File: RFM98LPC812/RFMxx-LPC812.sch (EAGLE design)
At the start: 33 parts, among them X1 BU-SMA-V, X2 BU-SMA-V

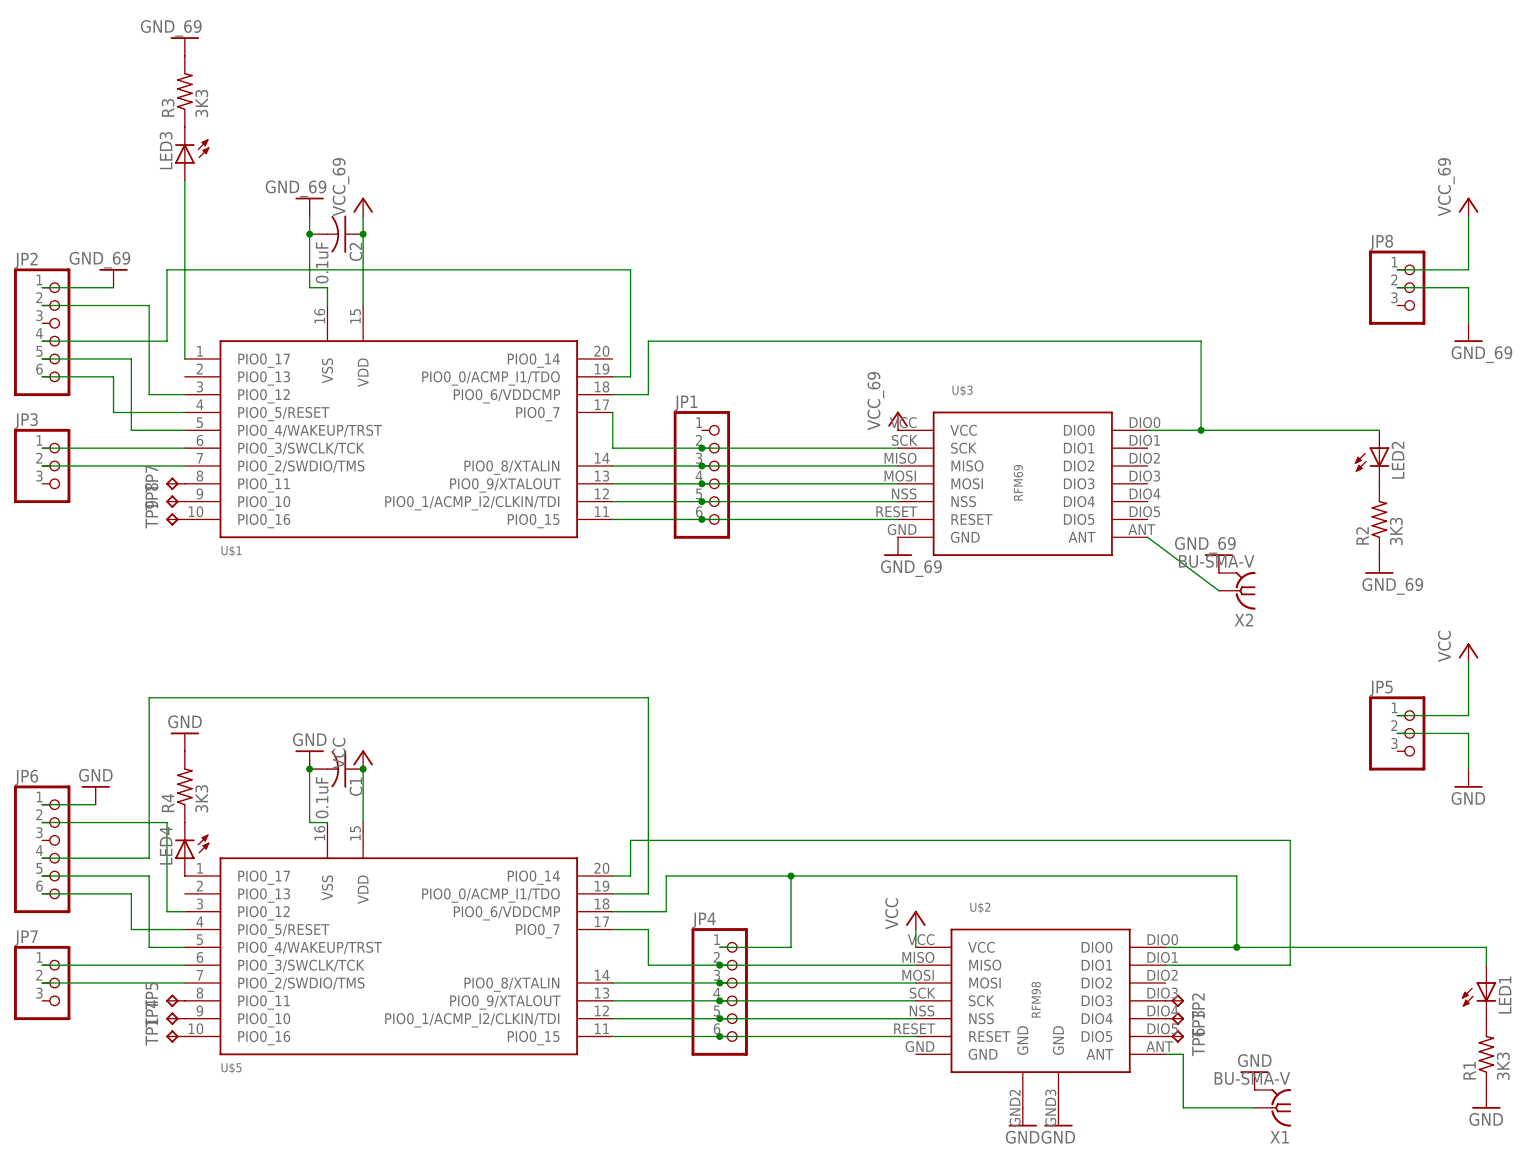
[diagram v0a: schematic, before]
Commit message: added TPs for DIO0..5 on RFM69 side
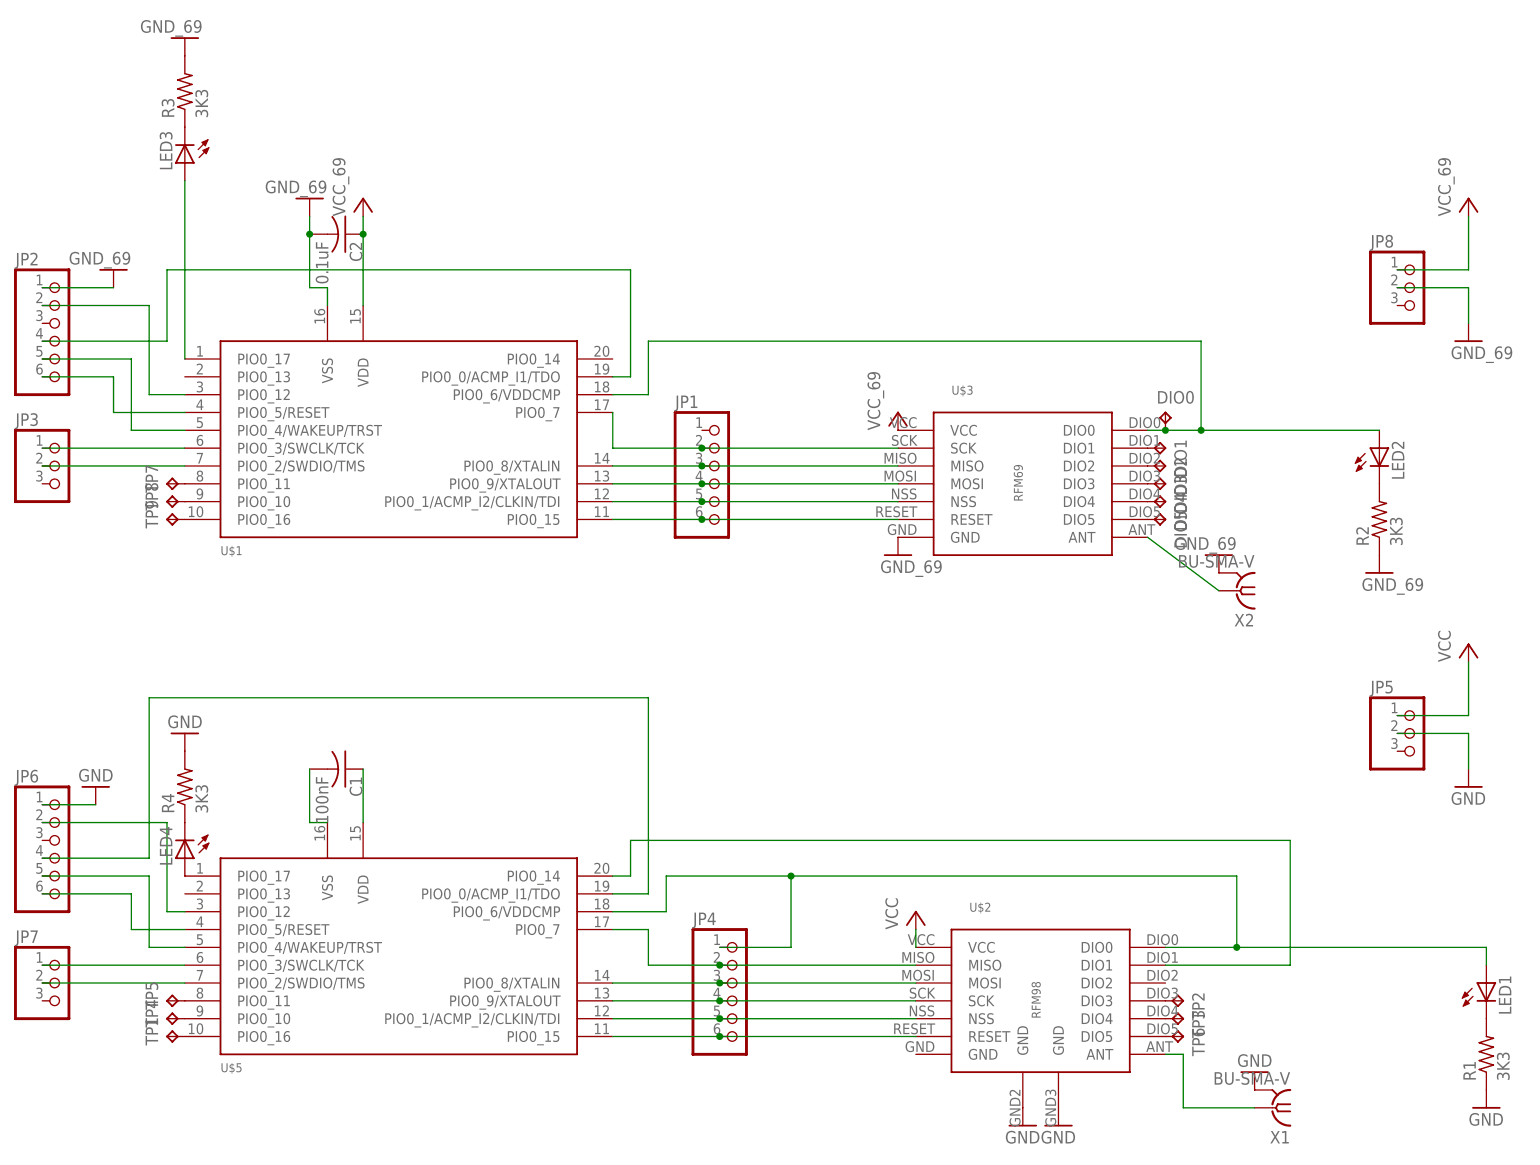
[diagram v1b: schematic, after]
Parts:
- added DIO0, DIO1, DIO2, DIO3, DIO4, DIO5: TPB1,27, testpad:TPB1,27
- C1: value 0.1uF -> 100nF
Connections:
- new net N$45: C1.2, U$5.VSS
- new net N$46: C1.1, U$5.VDD
- new net N$47: DIO1.TP, U$3.DIO1
- new net N$48: DIO2.TP, U$3.DIO2
- new net N$49: DIO3.TP, U$3.DIO3
- new net N$50: DIO4.TP, U$3.DIO4
- new net N$51: DIO5.TP, U$3.DIO5
- net GND: no longer C1.2, U$5.VSS
- net N$24: now also DIO0.TP
- net VCC: no longer C1.1, U$5.VDD
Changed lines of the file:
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@@
 <setting verticaltext="up"/>
 </settings>
-<grid distance="0.1" unitdist="inch" unit="inch" style="lines" multiple="1" display="yes" altdistance="0.01" altunitdist="inch" altunit="inch"/>
+<grid distance="0.1" unitdist="inch" unit="inch" style="lines" multiple="1" display="no" altdistance="0.01" altunitdist="inch" altunit="inch"/>
 <layers>
 <layer number="1" name="Top" color="4" fill="1" visible="no" active="no"/>
@@
 <part name="U$5" library="LPC812" deviceset="LPC812M101JD20" device=""/>
 <part name="JP4" library="adafruit" deviceset="PINHD-1X6" device=""/>
-<part name="P+1" library="supply1" deviceset="VCC" device=""/>
 <part name="JP5" library="adafruit" deviceset="PINHD-1X3" device=""/>
 <part name="P+3" library="supply1" deviceset="VCC" device=""/>
@@
 <part name="GND_RFM2" library="supply1" deviceset="GND" device=""/>
 <part name="GND_RFM3" library="supply1" deviceset="GND" device=""/>
-<part name="C1" library="adafruit" deviceset="C-US" device="C0805" value="0.1uF"/>
+<part name="C1" library="adafruit" deviceset="C-US" device="C0805" value="100nF"/>
 <part name="TP1" library="testpad" deviceset="TP" device="B1,27"/>
 <part name="JP7" library="adafruit" deviceset="PINHD-1X3" device=""/>
@@
 <part name="TP8" library="testpad" deviceset="TP" device="B1,27"/>
 <part name="TP9" library="testpad" deviceset="TP" device="B1,27"/>
-<part name="GND_RFM1" library="supply1" deviceset="GND" device=""/>
+<part name="DIO1" library="testpad" deviceset="TP" device="B1,27"/>
+<part name="DIO2" library="testpad" deviceset="TP" device="B1,27"/>
+<part name="DIO3" library="testpad" deviceset="TP" device="B1,27"/>
+<part name="DIO4" library="testpad" deviceset="TP" device="B1,27"/>
+<part name="DIO5" library="testpad" deviceset="TP" device="B1,27"/>
+<part name="DIO0" library="testpad" deviceset="TP" device="B1,27"/>
 </parts>
 <sheets>
@@
 <instance part="U$5" gate="G$1" x="-91.44" y="-27.94"/>
 <instance part="JP4" gate="A" x="-40.64" y="-33.02"/>
-<instance part="P+1" gate="VCC" x="-93.98" y="2.54"/>
 <instance part="JP5" gate="A" x="55.88" y="5.08"/>
 <instance part="P+3" gate="VCC" x="63.5" y="17.78"/>
@@
 <instance part="TP8" gate="G$1" x="-121.92" y="38.1" rot="R90"/>
 <instance part="TP9" gate="G$1" x="-121.92" y="35.56" rot="R90"/>
-<instance part="GND_RFM1" gate="1" x="-101.6" y="2.54" rot="R180"/>
+<instance part="DIO1" gate="G$1" x="20.32" y="45.72" rot="R270"/>
+<instance part="DIO2" gate="G$1" x="20.32" y="43.18" rot="R270"/>
+<instance part="DIO3" gate="G$1" x="20.32" y="40.64" rot="R270"/>
+<instance part="DIO4" gate="G$1" x="20.32" y="38.1" rot="R270"/>
+<instance part="DIO5" gate="G$1" x="20.32" y="35.56" rot="R270"/>
+<instance part="DIO0" gate="G$1" x="20.32" y="50.8"/>
 </instances>
 <busses>
@@
 <pinref part="P+3" gate="VCC" pin="VCC"/>
 <wire x1="63.5" y1="7.62" x2="63.5" y2="15.24" width="0.1524" layer="91"/>
-</segment>
-<segment>
-<pinref part="C1" gate="G$1" pin="1"/>
-<pinref part="P+1" gate="VCC" pin="VCC"/>
-<pinref part="U$5" gate="G$1" pin="VDD"/>
-<wire x1="-93.98" y1="-7.62" x2="-93.98" y2="0" width="0.1524" layer="91"/>
-<junction x="-93.98" y="0"/>
 </segment>
 <segment>
@@
 <pinref part="R4" gate="G$1" pin="2"/>
 <pinref part="GND_RFM6" gate="1" pin="GND"/>
-</segment>
-<segment>
-<pinref part="C1" gate="G$1" pin="2"/>
-<pinref part="U$5" gate="G$1" pin="VSS"/>
-<wire x1="-99.06" y1="-7.62" x2="-101.6" y2="-7.62" width="0.1524" layer="91"/>
-<wire x1="-101.6" y1="-7.62" x2="-101.6" y2="0" width="0.1524" layer="91"/>
-<pinref part="GND_RFM1" gate="1" pin="GND"/>
-<junction x="-101.6" y="0"/>
 </segment>
 </net>
@@
 <segment>
 <pinref part="U$3" gate="G$1" pin="DIO0"/>
-<wire x1="17.78" y1="48.26" x2="25.4" y2="48.26" width="0.1524" layer="91"/>
+<wire x1="17.78" y1="48.26" x2="20.32" y2="48.26" width="0.1524" layer="91"/>
+<wire x1="20.32" y1="48.26" x2="25.4" y2="48.26" width="0.1524" layer="91"/>
 <wire x1="25.4" y1="48.26" x2="25.4" y2="60.96" width="0.1524" layer="91"/>
 <wire x1="25.4" y1="60.96" x2="-53.34" y2="60.96" width="0.1524" layer="91"/>
@@
 <wire x1="25.4" y1="48.26" x2="50.8" y2="48.26" width="0.1524" layer="91"/>
 <junction x="25.4" y="48.26"/>
+<pinref part="DIO0" gate="G$1" pin="TP"/>
+<junction x="20.32" y="48.26"/>
 </segment>
 </net>
@@
 </segment>
 </net>
+<net name="N$45" class="0">
+<segment>
+<pinref part="C1" gate="G$1" pin="2"/>
+<wire x1="-101.6" y1="0" x2="-101.6" y2="-7.62" width="0.1524" layer="91"/>
+<pinref part="U$5" gate="G$1" pin="VSS"/>
+<wire x1="-101.6" y1="-7.62" x2="-99.06" y2="-7.62" width="0.1524" layer="91"/>
+</segment>
+</net>
+<net name="N$46" class="0">
+<segment>
+<pinref part="C1" gate="G$1" pin="1"/>
+<pinref part="U$5" gate="G$1" pin="VDD"/>
+<wire x1="-93.98" y1="0" x2="-93.98" y2="-7.62" width="0.1524" layer="91"/>
+</segment>
+</net>
+<net name="N$47" class="0">
+<segment>
+<pinref part="U$3" gate="G$1" pin="DIO1"/>
+<pinref part="DIO1" gate="G$1" pin="TP"/>
+</segment>
+</net>
+<net name="N$48" class="0">
+<segment>
+<pinref part="U$3" gate="G$1" pin="DIO2"/>
+<pinref part="DIO2" gate="G$1" pin="TP"/>
+</segment>
+</net>
+<net name="N$49" class="0">
+<segment>
+<pinref part="U$3" gate="G$1" pin="DIO3"/>
+<pinref part="DIO3" gate="G$1" pin="TP"/>
+</segment>
+</net>
+<net name="N$50" class="0">
+<segment>
+<pinref part="U$3" gate="G$1" pin="DIO4"/>
+<pinref part="DIO4" gate="G$1" pin="TP"/>
+</segment>
+</net>
+<net name="N$51" class="0">
+<segment>
+<pinref part="U$3" gate="G$1" pin="DIO5"/>
+<pinref part="DIO5" gate="G$1" pin="TP"/>
+</segment>
+</net>

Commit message: some refinements
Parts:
- added D_0, D_1, P14, TP12: TPB1,27, testpad:TPB1,27
- renumbered DIO0 to D0, DIO1 to D1, DIO2 to D2, DIO3 to D3, DIO4 to D4, DIO5 to D5, TP6 to D_5
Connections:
- removed net N$45: C1.2, U$5.VSS
- new net N$52: TP12.TP, U$2.DIO2
- net GND: now also C1.2, U$5.VSS
- net N$22: now also D_0.TP
- net N$27: now also D_1.TP
- net N$46: now also P14.TP, U$1.PIO0_14; no longer C1.1, U$5.VDD
- net VCC: now also C1.1, U$5.VDD
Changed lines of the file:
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@@
 <part name="TP4" library="testpad" deviceset="TP" device="B1,27"/>
 <part name="TP5" library="testpad" deviceset="TP" device="B1,27"/>
-<part name="TP6" library="testpad" deviceset="TP" device="B1,27"/>
+<part name="D_5" library="testpad" deviceset="TP" device="B1,27"/>
 <part name="GND1" library="supply1" deviceset="GND" device="" value="GND_69"/>
 <part name="C2" library="adafruit" deviceset="C-US" device="C0805" value="0.1uF"/>
@@
 <part name="TP8" library="testpad" deviceset="TP" device="B1,27"/>
 <part name="TP9" library="testpad" deviceset="TP" device="B1,27"/>
-<part name="DIO1" library="testpad" deviceset="TP" device="B1,27"/>
-<part name="DIO2" library="testpad" deviceset="TP" device="B1,27"/>
-<part name="DIO3" library="testpad" deviceset="TP" device="B1,27"/>
-<part name="DIO4" library="testpad" deviceset="TP" device="B1,27"/>
-<part name="DIO5" library="testpad" deviceset="TP" device="B1,27"/>
-<part name="DIO0" library="testpad" deviceset="TP" device="B1,27"/>
+<part name="D1" library="testpad" deviceset="TP" device="B1,27"/>
+<part name="D2" library="testpad" deviceset="TP" device="B1,27"/>
+<part name="D3" library="testpad" deviceset="TP" device="B1,27"/>
+<part name="D4" library="testpad" deviceset="TP" device="B1,27"/>
+<part name="D5" library="testpad" deviceset="TP" device="B1,27"/>
+<part name="D0" library="testpad" deviceset="TP" device="B1,27"/>
+<part name="D_0" library="testpad" deviceset="TP" device="B1,27"/>
+<part name="D_1" library="testpad" deviceset="TP" device="B1,27"/>
+<part name="TP12" library="testpad" deviceset="TP" device="B1,27"/>
+<part name="P+1" library="supply1" deviceset="VCC" device=""/>
+<part name="GND_RFM1" library="supply1" deviceset="GND" device=""/>
+<part name="P14" library="testpad" deviceset="TP" device="B1,27"/>
 </parts>
 <sheets>
@@
 <instance part="TP4" gate="G$1" x="-121.92" y="-35.56" rot="R90"/>
 <instance part="TP5" gate="G$1" x="-121.92" y="-33.02" rot="R90"/>
-<instance part="TP6" gate="G$1" x="22.86" y="-38.1" rot="R270"/>
+<instance part="D_5" gate="G$1" x="22.86" y="-38.1" rot="R270"/>
 <instance part="GND1" gate="1" x="-129.54" y="71.12" rot="R180"/>
 <instance part="C2" gate="G$1" x="-96.52" y="76.2" rot="R270"/>
@@
 <instance part="TP8" gate="G$1" x="-121.92" y="38.1" rot="R90"/>
 <instance part="TP9" gate="G$1" x="-121.92" y="35.56" rot="R90"/>
-<instance part="DIO1" gate="G$1" x="20.32" y="45.72" rot="R270"/>
-<instance part="DIO2" gate="G$1" x="20.32" y="43.18" rot="R270"/>
-<instance part="DIO3" gate="G$1" x="20.32" y="40.64" rot="R270"/>
-<instance part="DIO4" gate="G$1" x="20.32" y="38.1" rot="R270"/>
-<instance part="DIO5" gate="G$1" x="20.32" y="35.56" rot="R270"/>
-<instance part="DIO0" gate="G$1" x="20.32" y="50.8"/>
+<instance part="D1" gate="G$1" x="20.32" y="45.72" rot="R270"/>
+<instance part="D2" gate="G$1" x="20.32" y="43.18" rot="R270"/>
+<instance part="D3" gate="G$1" x="20.32" y="40.64" rot="R270"/>
+<instance part="D4" gate="G$1" x="20.32" y="38.1" rot="R270"/>
+<instance part="D5" gate="G$1" x="20.32" y="35.56" rot="R270"/>
+<instance part="D0" gate="G$1" x="20.32" y="50.8"/>
+<instance part="D_0" gate="G$1" x="25.4" y="-22.86"/>
+<instance part="D_1" gate="G$1" x="27.94" y="-25.4"/>
+<instance part="TP12" gate="G$1" x="22.86" y="-30.48" rot="R270"/>
+<instance part="P+1" gate="VCC" x="-93.98" y="2.54"/>
+<instance part="GND_RFM1" gate="1" x="-101.6" y="2.54" rot="R180"/>
+<instance part="P14" gate="G$1" x="-58.42" y="60.96"/>
 </instances>
 <busses>
@@
 <wire x1="53.34" y1="71.12" x2="63.5" y2="71.12" width="0.1524" layer="91"/>
 <wire x1="63.5" y1="71.12" x2="63.5" y2="78.74" width="0.1524" layer="91"/>
+</segment>
+<segment>
+<pinref part="C1" gate="G$1" pin="1"/>
+<pinref part="U$5" gate="G$1" pin="VDD"/>
+<wire x1="-93.98" y1="0" x2="-93.98" y2="-7.62" width="0.1524" layer="91"/>
+<pinref part="P+1" gate="VCC" pin="VCC"/>
+<junction x="-93.98" y="0"/>
 </segment>
 </net>
@@
 <pinref part="GND_RFM6" gate="1" pin="GND"/>
 </segment>
+<segment>
+<pinref part="C1" gate="G$1" pin="2"/>
+<wire x1="-101.6" y1="0" x2="-101.6" y2="-7.62" width="0.1524" layer="91"/>
+<pinref part="U$5" gate="G$1" pin="VSS"/>
+<wire x1="-101.6" y1="-7.62" x2="-99.06" y2="-7.62" width="0.1524" layer="91"/>
+<pinref part="GND_RFM1" gate="1" pin="GND"/>
+<junction x="-101.6" y="0"/>
+</segment>
 </net>
 <net name="N$11" class="0">
@@
 <wire x1="30.48" y1="-15.24" x2="30.48" y2="-25.4" width="0.1524" layer="91"/>
 <pinref part="U$2" gate="G$1" pin="DIO0"/>
-<wire x1="30.48" y1="-25.4" x2="20.32" y2="-25.4" width="0.1524" layer="91"/>
+<wire x1="30.48" y1="-25.4" x2="25.4" y2="-25.4" width="0.1524" layer="91"/>
+<wire x1="25.4" y1="-25.4" x2="20.32" y2="-25.4" width="0.1524" layer="91"/>
 <wire x1="-33.02" y1="-15.24" x2="-33.02" y2="-25.4" width="0.1524" layer="91"/>
 <pinref part="JP4" gate="A" pin="1"/>
@@
 <wire x1="66.04" y1="-25.4" x2="66.04" y2="-27.94" width="0.1524" layer="91"/>
 <junction x="30.48" y="-25.4"/>
+<pinref part="D_0" gate="G$1" pin="TP"/>
+<junction x="25.4" y="-25.4"/>
 </segment>
 </net>
@@
 <wire x1="38.1" y1="-10.16" x2="38.1" y2="-27.94" width="0.1524" layer="91"/>
 <pinref part="U$2" gate="G$1" pin="DIO1"/>
-<wire x1="38.1" y1="-27.94" x2="20.32" y2="-27.94" width="0.1524" layer="91"/>
+<wire x1="38.1" y1="-27.94" x2="27.94" y2="-27.94" width="0.1524" layer="91"/>
+<pinref part="D_1" gate="G$1" pin="TP"/>
+<wire x1="27.94" y1="-27.94" x2="20.32" y2="-27.94" width="0.1524" layer="91"/>
+<junction x="27.94" y="-27.94"/>
 </segment>
 </net>
@@
 <segment>
 <pinref part="U$2" gate="G$1" pin="DIO5"/>
-<pinref part="TP6" gate="G$1" pin="TP"/>
+<pinref part="D_5" gate="G$1" pin="TP"/>
 </segment>
 </net>
@@
 <wire x1="25.4" y1="48.26" x2="50.8" y2="48.26" width="0.1524" layer="91"/>
 <junction x="25.4" y="48.26"/>
-<pinref part="DIO0" gate="G$1" pin="TP"/>
+<pinref part="D0" gate="G$1" pin="TP"/>
 <junction x="20.32" y="48.26"/>
 </segment>
@@
 </segment>
 </net>
-<net name="N$45" class="0">
-<segment>
-<pinref part="C1" gate="G$1" pin="2"/>
-<wire x1="-101.6" y1="0" x2="-101.6" y2="-7.62" width="0.1524" layer="91"/>
-<pinref part="U$5" gate="G$1" pin="VSS"/>
-<wire x1="-101.6" y1="-7.62" x2="-99.06" y2="-7.62" width="0.1524" layer="91"/>
+<net name="N$47" class="0">
+<segment>
+<pinref part="U$3" gate="G$1" pin="DIO1"/>
+<pinref part="D1" gate="G$1" pin="TP"/>
+</segment>
+</net>
+<net name="N$48" class="0">
+<segment>
+<pinref part="U$3" gate="G$1" pin="DIO2"/>
+<pinref part="D2" gate="G$1" pin="TP"/>
+</segment>
+</net>
+<net name="N$49" class="0">
+<segment>
+<pinref part="U$3" gate="G$1" pin="DIO3"/>
+<pinref part="D3" gate="G$1" pin="TP"/>
+</segment>
+</net>
+<net name="N$50" class="0">
+<segment>
+<pinref part="U$3" gate="G$1" pin="DIO4"/>
+<pinref part="D4" gate="G$1" pin="TP"/>
+</segment>
+</net>
+<net name="N$51" class="0">
+<segment>
+<pinref part="U$3" gate="G$1" pin="DIO5"/>
+<pinref part="D5" gate="G$1" pin="TP"/>
+</segment>
+</net>
+<net name="N$52" class="0">
+<segment>
+<pinref part="U$2" gate="G$1" pin="DIO2"/>
+<pinref part="TP12" gate="G$1" pin="TP"/>
 </segment>
 </net>
 <net name="N$46" class="0">
 <segment>
-<pinref part="C1" gate="G$1" pin="1"/>
-<pinref part="U$5" gate="G$1" pin="VDD"/>
-<wire x1="-93.98" y1="0" x2="-93.98" y2="-7.62" width="0.1524" layer="91"/>
-</segment>
-</net>
-<net name="N$47" class="0">
-<segment>
-<pinref part="U$3" gate="G$1" pin="DIO1"/>
-<pinref part="DIO1" gate="G$1" pin="TP"/>
-</segment>
-</net>
-<net name="N$48" class="0">
-<segment>
-<pinref part="U$3" gate="G$1" pin="DIO2"/>
-<pinref part="DIO2" gate="G$1" pin="TP"/>
-</segment>
-</net>
-<net name="N$49" class="0">
-<segment>
-<pinref part="U$3" gate="G$1" pin="DIO3"/>
-<pinref part="DIO3" gate="G$1" pin="TP"/>
-</segment>
-</net>
-<net name="N$50" class="0">
-<segment>
-<pinref part="U$3" gate="G$1" pin="DIO4"/>
-<pinref part="DIO4" gate="G$1" pin="TP"/>
-</segment>
-</net>
-<net name="N$51" class="0">
-<segment>
-<pinref part="U$3" gate="G$1" pin="DIO5"/>
-<pinref part="DIO5" gate="G$1" pin="TP"/>
-</segment>
-</net>
+<pinref part="U$1" gate="G$1" pin="PIO0_14"/>
+<pinref part="P14" gate="G$1" pin="TP"/>
+</segment>
+</net>
